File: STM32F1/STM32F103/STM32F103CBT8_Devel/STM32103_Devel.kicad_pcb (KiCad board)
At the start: 4 copper layers, 69 x 50 mm, 47 parts, among them J1 Conn_02x03_Counter_Clockwise, J2 USB_B_Micro, J3 Conn_02x03_Counter_Clockwise, J4 Conn_01x16, J5 Conn_01x16, J6 Conn_02x05 Odd_Even, SW1 SW_Push, SW2 SW_DIP_x02, U1 STM32F103CBTx, U2 AMS1117-3.3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

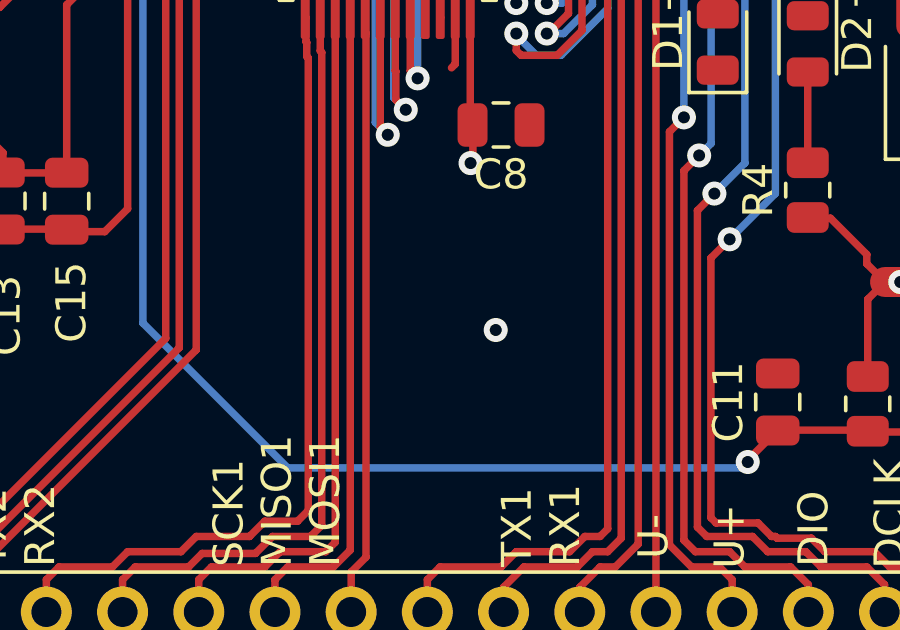
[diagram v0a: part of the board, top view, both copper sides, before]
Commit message: I2C pull-Up
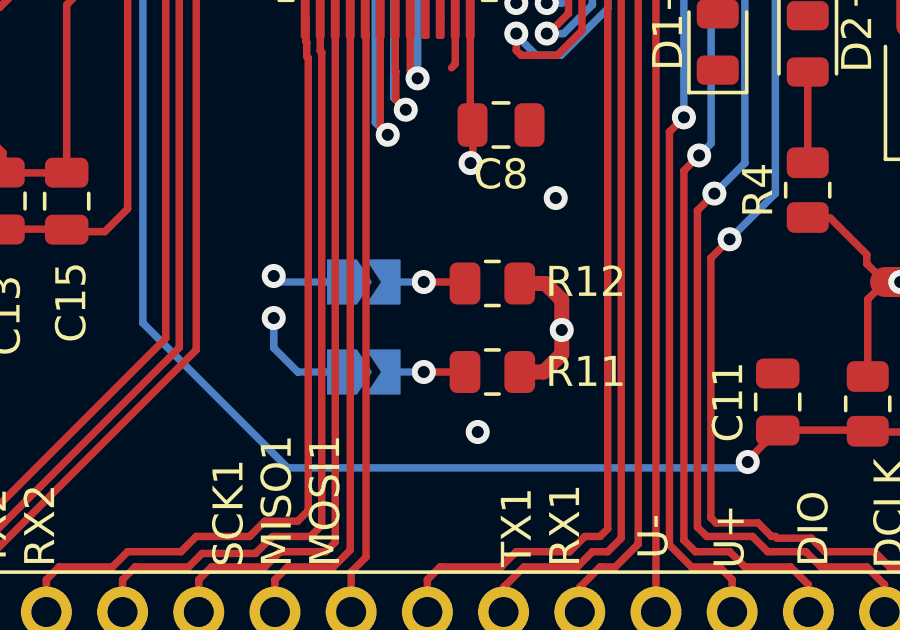
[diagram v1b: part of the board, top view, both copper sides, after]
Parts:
- added JP1: sj_o, Jumper:SolderJumper-2_P1.3mm_Open_TrianglePad1.0x1.5mm, B.Cu at (127.2, 105.0)
- added JP2: sj_o, Jumper:SolderJumper-2_P1.3mm_Open_TrianglePad1.0x1.5mm, B.Cu at (127.2, 108.0)
- added R11: 10K, Resistor_SMD:R_0805_2012Metric, F.Cu at (131.5, 108.0)
- added R12: 10K, Resistor_SMD:R_0805_2012Metric, F.Cu at (131.5, 105.0)
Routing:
- net /PB6: track 24.7 -> 54.8 mm, vias 1 -> 2
- net /PB7: track 22.2 -> 48.1 mm, vias 1 -> 2
- net VCC: track 59.3 -> 64.4 mm, vias 13 -> 14
- net Net-(JP1-B): track 0.00 -> 2.67 mm, vias 0 -> 1
- net Net-(JP2-B): track 0.00 -> 2.65 mm, vias 0 -> 1
- net GND: vias 9 -> 10

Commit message: Docu Actualizada + info silk
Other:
- board text added: "STM32F103 v 0.0.3"
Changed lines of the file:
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@@
 		(layer "Margin")
+	)
+	(gr_text "STM32F103\nv 0.0.3"
+		(at 148 93.6 -0)
+		(layer "B.SilkS")
+		(effects
+			(font
+				(size 1 1)
+				(thickness 0.15)
+			)
+			(justify left bottom mirror)
+		)
 	)
 	(gr_text "SCK2\nMISO2\nMOSI2"
@@
 		)
 	)
+	(gr_text "STM32F103\nv 0.0.3"
+		(at 120 103.2 0)
+		(layer "F.SilkS")
+		(effects
+			(font
+				(size 1 1)
+				(thickness 0.15)
+			)
+			(justify left bottom)
+		)
+	)

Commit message: 6Pin conector debug
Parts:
- added J7: Conn_01x06, Connector_PinHeader_2.54mm:PinHeader_1x06_P2.54mm_Vertical, F.Cu at (166.5, 95.9)
- moved J1 52.2 mm to (112.1, 108.8), turned to -90 degrees
- moved J3 22.6 mm to (153.0, 76.3), turned to 90 degrees
- moved J6 5.81 mm to (159.5, 103.5)
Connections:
- J2 pad 4: unconnected-(J2-ID-Pad4) -> Net-(J2-ID)
- R7 pad 1: unconnected-(J2-ID-Pad4) -> Net-(J2-ID)
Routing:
- net /STM32F103CB/RST: track 78.6 -> 89.0 mm, vias 2 -> 3
- net /PB3: track 76.3 -> 86.0 mm
- net /PA14: track 86.8 -> 95.9 mm, vias 3 -> 4
- net /PA13: track 81.4 -> 90.2 mm
- net unconnected-(J2-ID-Pad4): track 5.68 -> 0.00 mm
- net Net-(J2-ID): track 0.00 -> 5.68 mm
- net +5V: track 35.1 -> 36.8 mm, vias 0 -> 1
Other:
- board text added: "3.3V GND"
- board text added: "5V"
- board text added: "VCC DCLK"
- board text added: "VCC DCLK GND DIO RST SWO"
- board text removed: "3.3V"
- board text removed: "5V GND"
